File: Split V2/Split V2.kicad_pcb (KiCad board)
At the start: 2 copper layers, 165.9 x 121.3 mm, 63 parts, among them J1 AudioJack4

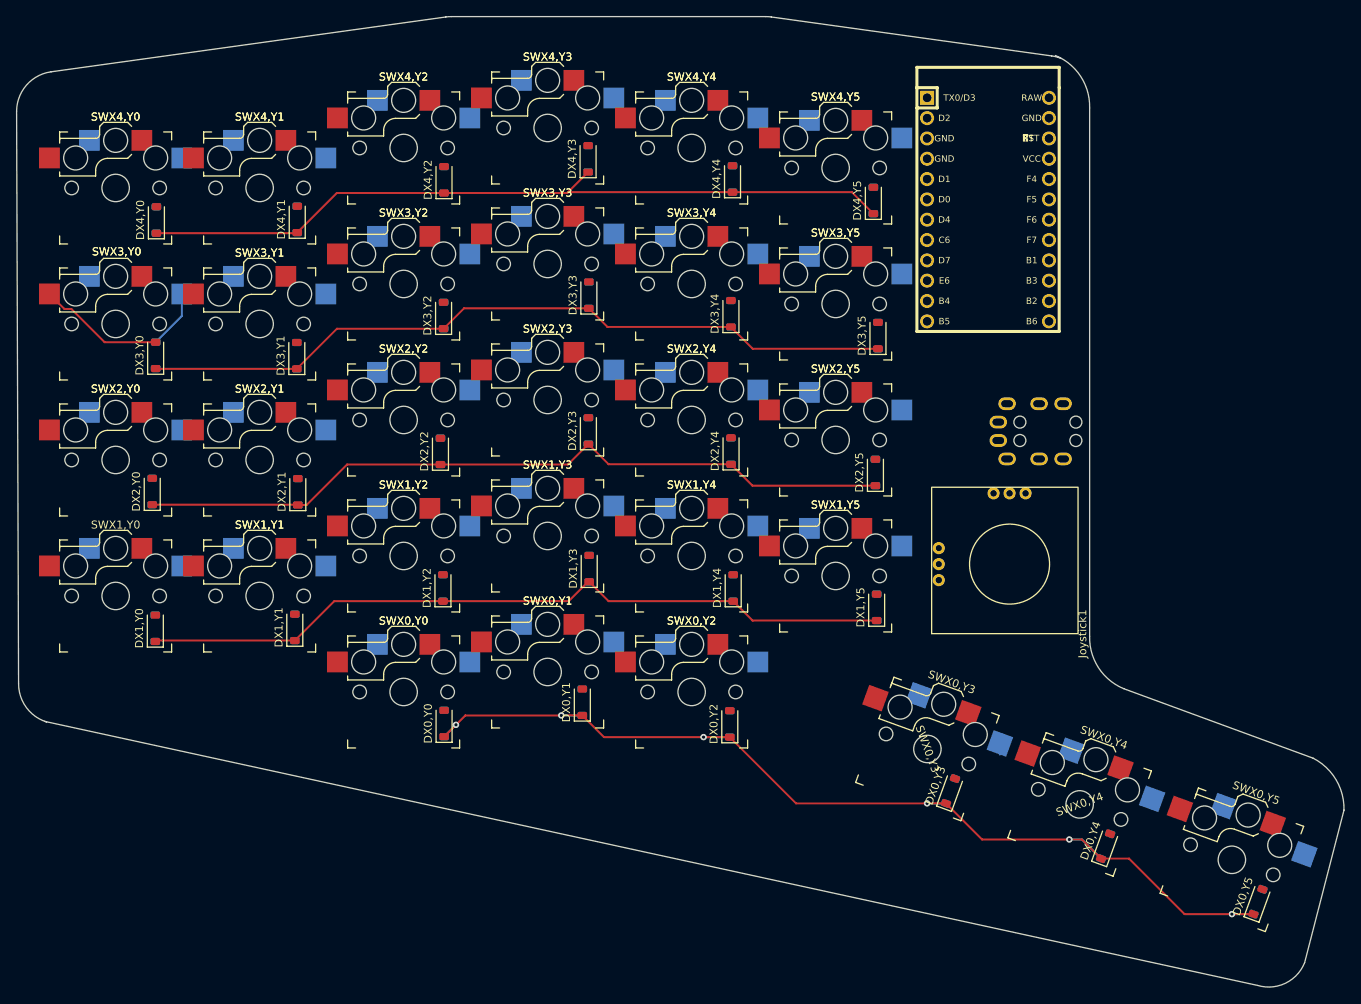
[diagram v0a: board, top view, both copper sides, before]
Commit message: V1 Traces
Got all of my traces layed out and worked on creating the reversable footprint like in other projects. Need to do some more research as to the specifics
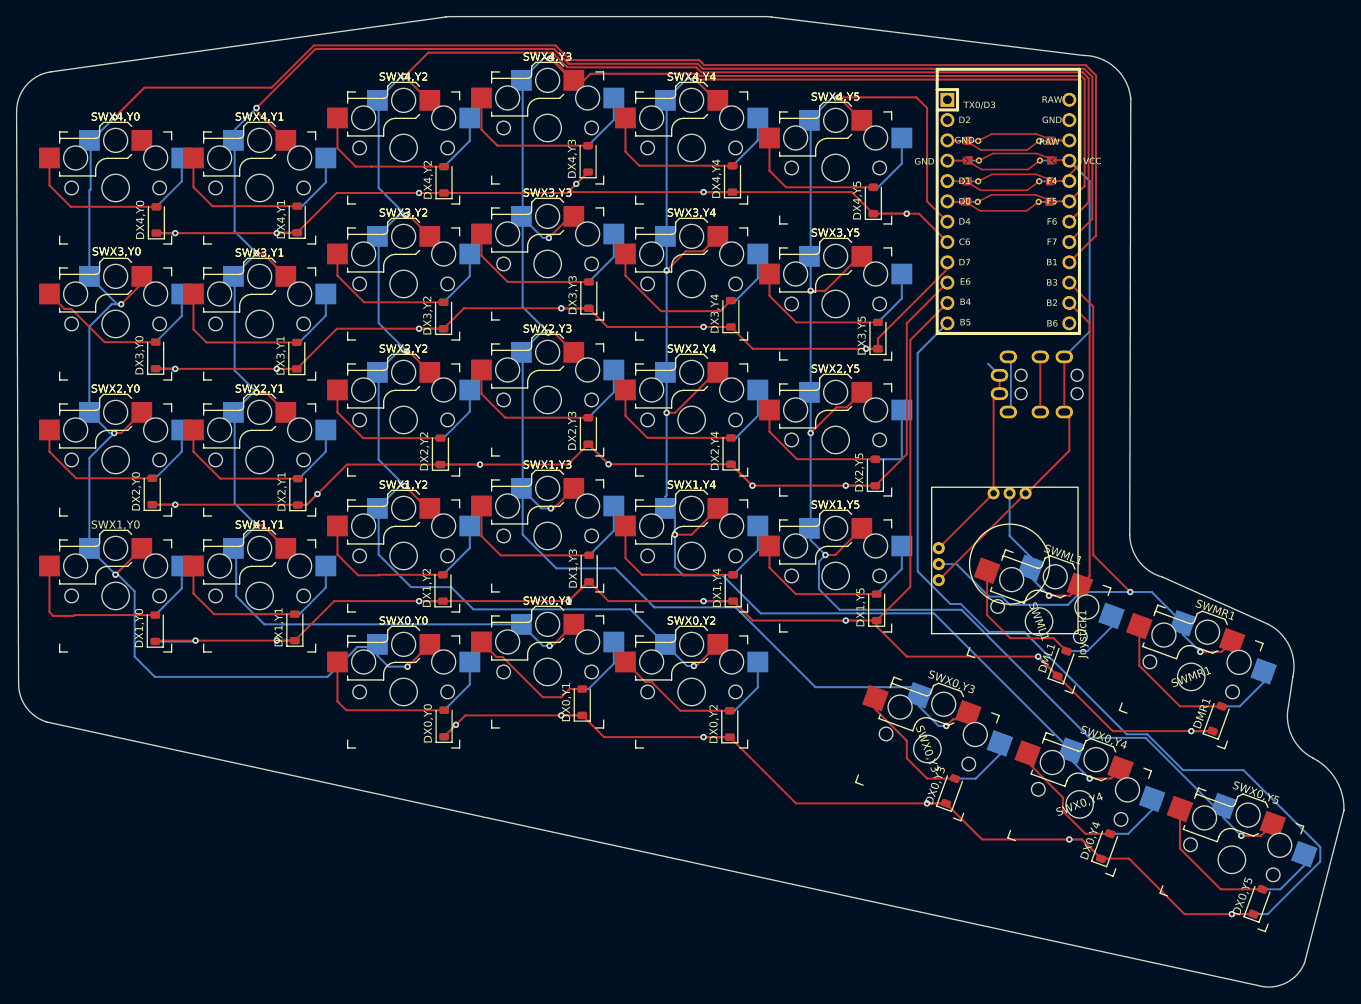
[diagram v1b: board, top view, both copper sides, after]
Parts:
- added DML1: ~, Custom:D_SOD-123_bothside, F.Cu at (209.9, 135.5)
- added DMR1: ~, Custom:D_SOD-123_bothside, F.Cu at (229.3, 142.4)
- added SWML1: ~, keyswitches.pretty-master:Kailh_socket_PG1350_optional_reversible, F.Cu at (207.0, 130.2)
- added SWMR1: ~, keyswitches.pretty-master:Kailh_socket_PG1350_optional_reversible, F.Cu at (226.1, 137.2)
- moved J1 5.86 mm to (213.4, 101.8)
- moved ProMicro1 2.55 mm to (203.2, 79.0), turned to 0 degrees
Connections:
- net Net-(Joystick1-DataX) renamed B2
- net Net-(Joystick1-DataY) renamed B3
- J1 pad 2: SDA -> SCL
- J1 pad 3: SCL -> SDA
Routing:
- net Col0: track 0.00 -> 288.1 mm, vias 0 -> 5
- net Col1: track 0.00 -> 266.4 mm, vias 0 -> 5
- net Col2: track 0.00 -> 244.8 mm, vias 0 -> 5
- net Col3: track 0.00 -> 243.2 mm, vias 0 -> 5
- net Col4: track 0.00 -> 220.4 mm, vias 0 -> 5
- net Col5: track 0.00 -> 191.7 mm, vias 0 -> 5
- net Row1: track 95.3 -> 214.3 mm, vias 0 -> 8
- net Row0: track 130.6 -> 240.6 mm
- net B3: track 0.00 -> 85.7 mm, vias 0 -> 2
- net VCC: track 0.00 -> 61.9 mm
- net B2: track 0.00 -> 56.1 mm, vias 0 -> 1
- net Row2: track 95.7 -> 146.7 mm, vias 0 -> 6
- net Row3: track 95.5 -> 126.3 mm, vias 0 -> 6
- net Row4: track 96.6 -> 125.2 mm, vias 0 -> 6
- net Gnd: track 0.00 -> 26.8 mm
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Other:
- outline, holes or cut-outs redrawn
